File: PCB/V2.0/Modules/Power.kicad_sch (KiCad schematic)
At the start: 16 parts, among them J1 Screw_Terminal_01x04, J30 Servo, J32 Power_Servo_Selector, J33 Screw_Terminal_01x02, J34 Sig_Servo, J37 Sig_MOSFET, Q1 IRF520, Q2 2N7002, SW5 SW_Left, U2 PC817

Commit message: Add RTC
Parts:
- added J26: Servo, Connector_PinHeader_2.54mm:PinHeader_1x03_P2.54mm_Vertical, symbol Connector:Conn_01x03_Pin
- added J29: Sig_Servo, Connector_PinHeader_2.54mm:PinHeader_1x01_P2.54mm_Vertical, symbol Connector:Conn_01x01_Pin
- R12, R13, R14, R17, R9: footprint Resistor_THT:R_Axial_DIN0207_L6.3mm_D2.5mm_P7.62mm_Horizontal -> Resistor_THT:R_Axial_DIN0207_L6.3mm_D2.5mm_P10.16mm_Horizontal
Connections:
- net GND: now also J26.3 (Pin_3)
- net at J30.2 (Pin_2), J32.2 (Pin_2): now also J26.2 (Pin_2)
- new net: J26.1 (Pin_1), J29.1 (Pin_1)
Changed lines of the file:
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@@
+	)
+	(junction
+		(at 76.2 92.71)
+		(diameter 0)
+		(color 0 0 0 0)
 	)
 	(junction
@@
 	(wire
 		(pts
+			(xy 55.88 105.41) (xy 57.15 105.41)
+		)
+		(stroke
+			(width 0)
+			(type default)
+		)
+	)
+	(wire
+		(pts
 			(xy 71.12 86.36) (xy 73.66 86.36)
 		)
@@
 	(wire
 		(pts
+			(xy 55.88 110.49) (xy 62.23 110.49)
+		)
+		(stroke
+			(width 0)
+			(type default)
+		)
+	)
+	(wire
+		(pts
 			(xy 100.33 31.75) (xy 101.6 31.75)
 		)
@@
 	(wire
 		(pts
+			(xy 76.2 107.95) (xy 76.2 92.71)
+		)
+		(stroke
+			(width 0)
+			(type default)
+		)
+	)
+	(wire
+		(pts
 			(xy 55.88 95.25) (xy 62.23 95.25)
 		)
@@
 		(pts
 			(xy 55.88 90.17) (xy 58.42 90.17)
+		)
+		(stroke
+			(width 0)
+			(type default)
+		)
+	)
+	(wire
+		(pts
+			(xy 55.88 107.95) (xy 76.2 107.95)
 		)
 		(stroke
@@
 	(label "GND"
 		(at 39.37 66.04 0)
+		(fields_autoplaced yes)
+		(effects
+			(font
+				(size 1.27 1.27)
+			)
+			(justify left bottom)
+		)
+	)
+	(label "GND"
+		(at 62.23 110.49 0)
 		(fields_autoplaced yes)
 		(effects
@@
 			)
 		)
-		(property "Footprint" "Resistor_THT:R_Axial_DIN0207_L6.3mm_D2.5mm_P7.62mm_Horizontal"
+		(property "Footprint" "Resistor_THT:R_Axial_DIN0207_L6.3mm_D2.5mm_P10.16mm_Horizontal"
 			(at 41.148 59.69 90)
 			(effects
@@
 			)
 		)
-		(property "Footprint" "Resistor_THT:R_Axial_DIN0207_L6.3mm_D2.5mm_P7.62mm_Horizontal"
+		(property "Footprint" "Resistor_THT:R_Axial_DIN0207_L6.3mm_D2.5mm_P10.16mm_Horizontal"
 			(at 41.148 38.1 90)
 			(effects
@@
 				(path "/8bcd0d00-b75f-4070-8d50-196a2022a31c/e1d3bd42-1f6e-4b6a-91f5-e751dfb804bc"
 					(reference "D5")
+					(unit 1)
+				)
+			)
+		)
+	)
+	(symbol
+		(lib_id "Connector:Conn_01x03_Pin")
+		(at 50.8 107.95 0)
+		(unit 1)
+		(exclude_from_sim no)
+		(in_bom yes)
+		(on_board yes)
+		(dnp no)
+		(fields_autoplaced yes)
+		(property "Reference" "J26"
+			(at 51.435 100.33 0)
+			(effects
+				(font
+					(size 1.27 1.27)
+				)
+			)
+		)
+		(property "Value" "Servo"
+			(at 51.435 102.87 0)
+			(effects
+				(font
+					(size 1.27 1.27)
+				)
+			)
+		)
+		(property "Footprint" "Connector_PinHeader_2.54mm:PinHeader_1x03_P2.54mm_Vertical"
+			(at 50.8 107.95 0)
+			(effects
+				(font
+					(size 1.27 1.27)
+				)
+				(hide yes)
+			)
+		)
+		(property "Datasheet" "~"
+			(at 50.8 107.95 0)
+			(effects
+				(font
+					(size 1.27 1.27)
+				)
+				(hide yes)
+			)
+		)
+		(property "Description" "Generic connector, single row, 01x03, script generated"
+			(at 50.8 107.95 0)
+			(effects
+				(font
+					(size 1.27 1.27)
+				)
+				(hide yes)
+			)
+		)
+		(pin "2"
+		)
+		(pin "3"
+		)
+		(pin "1"
+		)
+		(instances
+			(project "CREPP.io"
+				(path "/8bcd0d00-b75f-4070-8d50-196a2022a31c/e1d3bd42-1f6e-4b6a-91f5-e751dfb804bc"
+					(reference "J26")
 					(unit 1)
 				)
@@
 			)
 		)
-		(property "Footprint" "Resistor_THT:R_Axial_DIN0207_L6.3mm_D2.5mm_P7.62mm_Horizontal"
+		(property "Footprint" "Resistor_THT:R_Axial_DIN0207_L6.3mm_D2.5mm_P10.16mm_Horizontal"
 			(at 61.468 43.18 90)
 			(effects
@@
 	)
 	(symbol
+		(lib_id "Connector:Conn_01x01_Pin")
+		(at 62.23 105.41 180)
+		(unit 1)
+		(exclude_from_sim no)
+		(in_bom yes)
+		(on_board yes)
+		(dnp no)
+		(property "Reference" "J29"
+			(at 64.262 105.41 0)
+			(effects
+				(font
+					(size 1.27 1.27)
+				)
+			)
+		)
+		(property "Value" "Sig_Servo"
+			(at 61.595 102.87 0)
+			(effects
+				(font
+					(size 1.27 1.27)
+				)
+			)
+		)
+		(property "Footprint" "Connector_PinHeader_2.54mm:PinHeader_1x01_P2.54mm_Vertical"
+			(at 62.23 105.41 0)
+			(effects
+				(font
+					(size 1.27 1.27)
+				)
+				(hide yes)
+			)
+		)
+		(property "Datasheet" "~"
+			(at 62.23 105.41 0)
+			(effects
+				(font
+					(size 1.27 1.27)
+				)
+				(hide yes)
+			)
+		)
+		(property "Description" "Generic connector, single row, 01x01, script generated"
+			(at 62.23 105.41 0)
+			(effects
+				(font
+					(size 1.27 1.27)
+				)
+				(hide yes)
+			)
+		)
+		(pin "1"
+		)
+		(instances
+			(project "CREPP.io"
+				(path "/8bcd0d00-b75f-4070-8d50-196a2022a31c/e1d3bd42-1f6e-4b6a-91f5-e751dfb804bc"
+					(reference "J29")
+					(unit 1)
+				)
+			)
+		)
+	)
+	(symbol
 		(lib_id "Device:R")
 		(at 81.28 50.8 0)
@@
 			)
 		)
-		(property "Footprint" "Resistor_THT:R_Axial_DIN0207_L6.3mm_D2.5mm_P7.62mm_Horizontal"
+		(property "Footprint" "Resistor_THT:R_Axial_DIN0207_L6.3mm_D2.5mm_P10.16mm_Horizontal"
 			(at 79.502 50.8 90)
 			(effects
@@
 			)
 		)
-		(property "Footprint" "Resistor_THT:R_Axial_DIN0207_L6.3mm_D2.5mm_P7.62mm_Horizontal"
+		(property "Footprint" "Resistor_THT:R_Axial_DIN0207_L6.3mm_D2.5mm_P10.16mm_Horizontal"
 			(at 79.502 38.1 90)
 			(effects

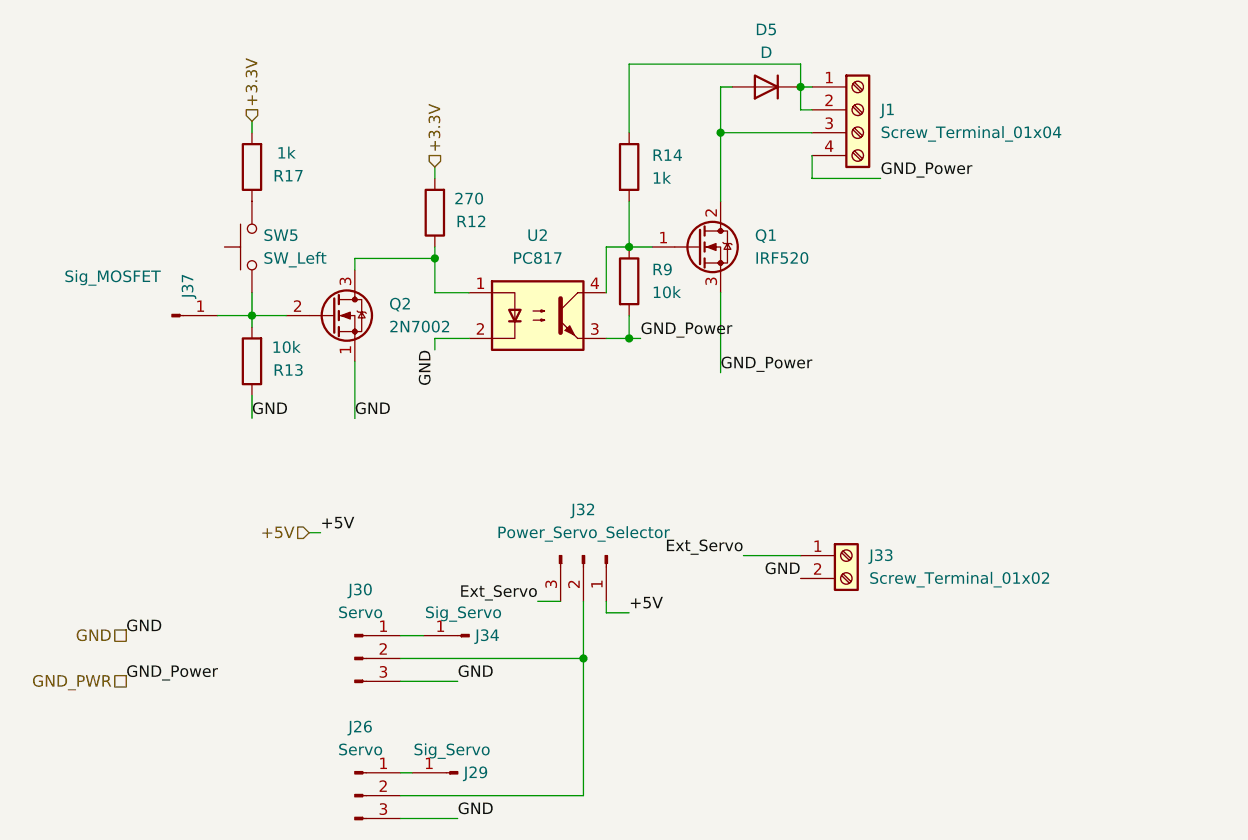
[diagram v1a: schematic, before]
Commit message: Update V2.0 form factor
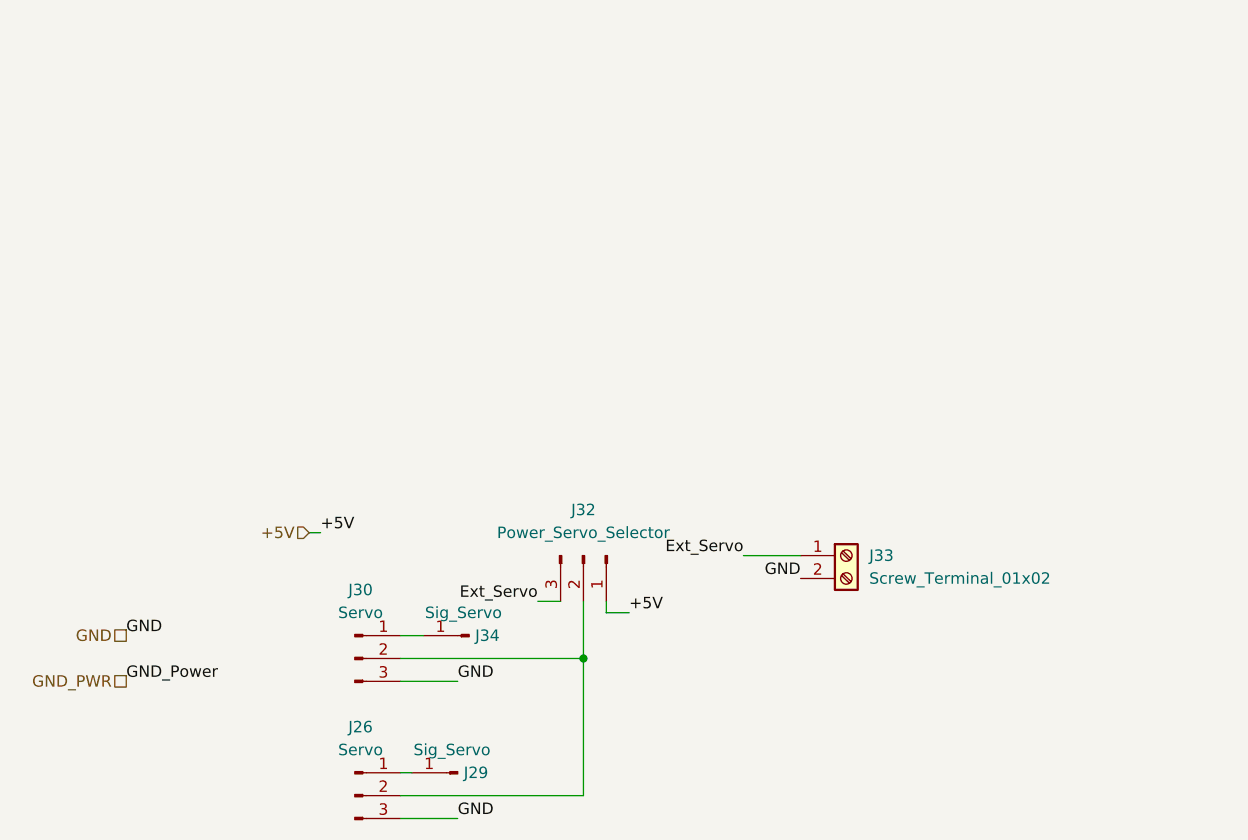
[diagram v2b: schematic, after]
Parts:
- removed D5: D, Diode_THT:D_A-405_P7.62mm_Horizontal, symbol Device:D
- removed J1: Screw_Terminal_01x04, TerminalBlock_Phoenix:TerminalBlock_Phoenix_MKDS-1,5-4-5.08_1x04_P5.08mm_Horizontal, symbol Connector:Screw_Terminal_01x04
- removed J37: Sig_MOSFET, Connector_PinHeader_2.54mm:PinHeader_1x01_P2.54mm_Vertical, symbol Connector:Conn_01x01_Pin
- removed Q1: IRF520, Package_TO_SOT_THT:TO-220-3_Vertical, symbol Transistor_FET:IRF540N
- removed Q2: 2N7002, Package_TO_SOT_THT:TO-92_Inline, symbol Transistor_FET:2N7000
- removed R12: 270, Resistor_THT:R_Axial_DIN0207_L6.3mm_D2.5mm_P10.16mm_Horizontal, symbol Device:R
- removed R13, R9: 10k, Resistor_THT:R_Axial_DIN0207_L6.3mm_D2.5mm_P10.16mm_Horizontal, symbol Device:R
- removed R14, R17: 1k, Resistor_THT:R_Axial_DIN0207_L6.3mm_D2.5mm_P10.16mm_Horizontal, symbol Device:R
- removed SW5: SW_Left, Button_Switch_THT:SW_PUSH_6mm, symbol Switch:SW_Push
- removed U2: PC817, Package_DIP:DIP-4_W7.62mm, symbol Isolator:PC817
- J33: footprint TerminalBlock_Phoenix:TerminalBlock_Phoenix_MKDS-1,5-2_1x02_P5.00mm_Horizontal -> TerminalBlock_Phoenix:TerminalBlock_Phoenix_MKDS-3-2-5.08_1x02_P5.08mm_Horizontal

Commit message: Add img
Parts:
- added JP30: Jumper_2.54mm_red, CREPP_Jumpers:Jumper_2.54mm_red, symbol CREPP_Jumpers:Jumper_2.54mm_red
- added M3: Motor_DC, Connector_PinHeader_2.54mm:PinHeader_1x01_P2.54mm_Vertical, symbol Motor:Motor_DC
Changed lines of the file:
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@@
+	)
+	(symbol
+		(lib_id "Motor:Motor_DC")
+		(at 132.08 95.25 0)
+		(unit 1)
+		(exclude_from_sim no)
+		(in_bom yes)
+		(on_board yes)
+		(dnp no)
+		(fields_autoplaced yes)
+		(property "Reference" "M3"
+			(at 137.16 96.5199 0)
+			(effects
+				(font
+					(size 1.27 1.27)
+				)
+				(justify left)
+			)
+		)
+		(property "Value" "Motor_DC"
+			(at 137.16 99.0599 0)
+			(effects
+				(font
+					(size 1.27 1.27)
+				)
+				(justify left)
+			)
+		)
+		(property "Footprint" "Connector_PinHeader_2.54mm:PinHeader_1x01_P2.54mm_Vertical"
+			(at 132.08 97.536 0)
+			(effects
+				(font
+					(size 1.27 1.27)
+				)
+				(hide yes)
+			)
+		)
+		(property "Datasheet" "~"
+			(at 132.08 97.536 0)
+			(effects
+				(font
+					(size 1.27 1.27)
+				)
+				(hide yes)
+			)
+		)
+		(property "Description" "DC Motor"
+			(at 132.08 95.25 0)
+			(effects
+				(font
+					(size 1.27 1.27)
+				)
+				(hide yes)
+			)
+		)
+		(pin "2"
+		)
+		(pin "1"
+		)
+		(instances
+			(project "CREPP.io"
+				(path "/8bcd0d00-b75f-4070-8d50-196a2022a31c/e1d3bd42-1f6e-4b6a-91f5-e751dfb804bc"
+					(reference "M3")
+					(unit 1)
+				)
+			)
+		)
+	)
+	(symbol
+		(lib_id "CREPP_Jumpers:Jumper_2.54mm_red")
+		(at 77.47 73.66 0)
+		(unit 1)
+		(exclude_from_sim yes)
+		(in_bom yes)
+		(on_board yes)
+		(dnp no)
+		(fields_autoplaced yes)
+		(property "Reference" "JP30"
+			(at 81.28 73.0249 0)
+			(effects
+				(font
+					(size 1.27 1.27)
+				)
+				(justify left)
+			)
+		)
+		(property "Value" "Jumper_2.54mm_red"
+			(at 77.47 75.946 0)
+			(effects
+				(font
+					(size 1.27 1.27)
+				)
+				(hide yes)
+			)
+		)
+		(property "Footprint" "CREPP_Jumpers:Jumper_2.54mm_red"
+			(at 77.47 73.66 0)
+			(effects
+				(font
+					(size 1.27 1.27)
+				)
+				(hide yes)
+			)
+		)
+		(property "Datasheet" "~"
+			(at 77.47 73.66 0)
+			(effects
+				(font
+					(size 1.27 1.27)
+				)
+				(hide yes)
+			)
+		)
+		(property "Description" "Jumper, 2-pole, open"
+			(at 77.47 73.66 0)
+			(effects
+				(font
+					(size 1.27 1.27)
+				)
+				(hide yes)
+			)
+		)
+		(instances
+			(project "CREPP.io"
+				(path "/8bcd0d00-b75f-4070-8d50-196a2022a31c/e1d3bd42-1f6e-4b6a-91f5-e751dfb804bc"
+					(reference "JP30")
+					(unit 1)
+				)
+			)
+		)
 	)
 	(symbol
